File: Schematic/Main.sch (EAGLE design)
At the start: 68 parts, among them IC1 PIC18F4550_40, IC2 7805, IC4 AD7734, IC5 AD780, K1 SRD-24VDC-SL-C, K2 SRD-24VDC-SL-C, Q1 20MHz, Q2 3.579545MHz, T1 2N2222, U1 LM317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

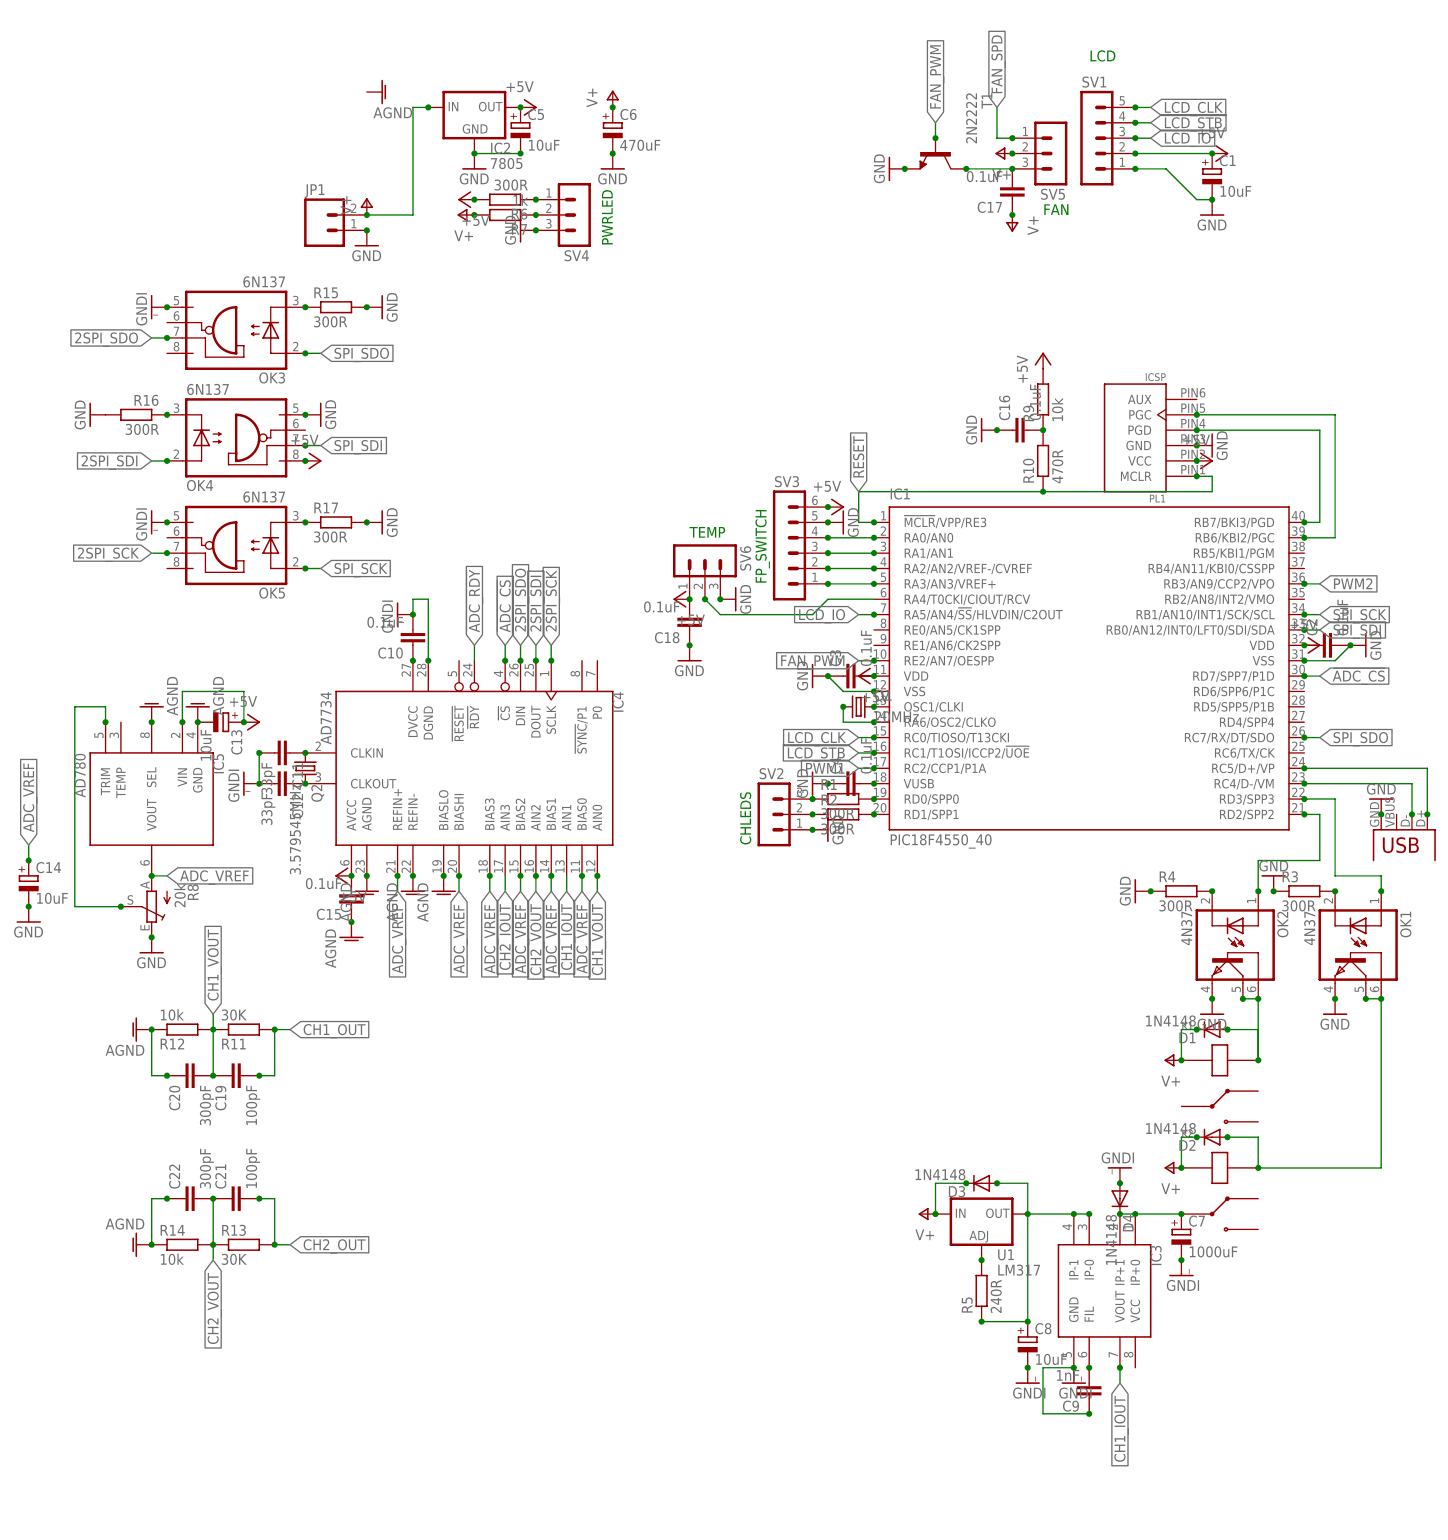
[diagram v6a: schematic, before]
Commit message: Added optocouplers to isolate output stuff; need separate PSU for µC stuff, second channel.
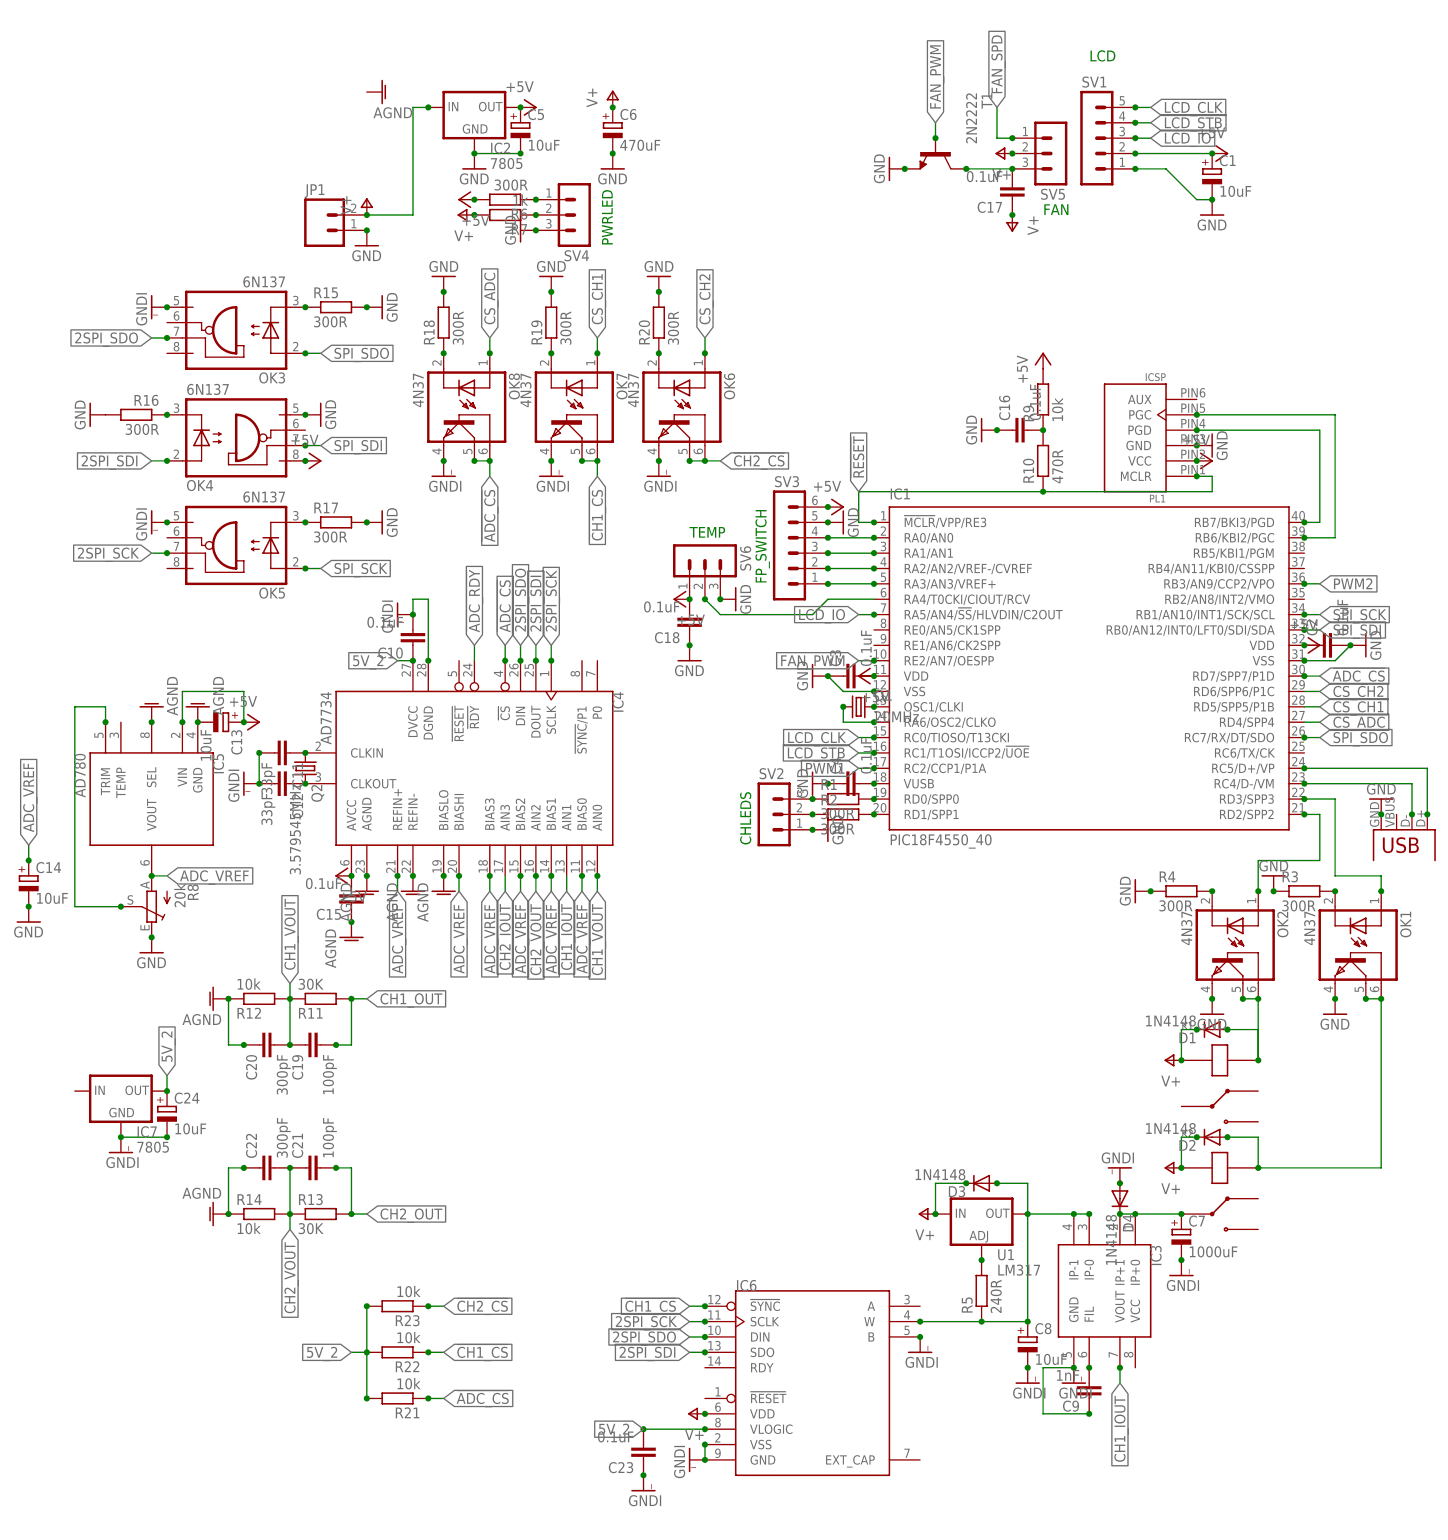
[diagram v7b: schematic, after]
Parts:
- added C23: 0.1uF, rcl:C-EU025-030X050
- added C24: 10uF, rcl:CPOL-EUE2.5-5
- added IC6: (no value), Particulates:AD5292TSSOP14
- added IC7: 7805, v-reg:78MXXS
- added OK6, OK7, OK8: 4N37, optocoupler:4N37
- added R18, R19, R20: 300R, rcl:R-EU_0204/7
- added R21, R22, R23: 10k, rcl:R-EU_0204/7
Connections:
- new net !CH1_CS!: IC6.!SYNC!, OK7.BAS, OK7.COL, R22.1
- new net !CH2_CS!: OK6.BAS, OK6.COL, R23.1
- new net 5V_2: C10.1, C23.2, C24.+, IC4.DVCC, IC6.VLOGIC, IC7.OUT, R21.2, R22.2, R23.2
- new net CS_ADC: IC1.RD4/SPP4, OK8.A
- new net CS_CH1: IC1.RD5/SPP5/P1B, OK7.A
- new net CS_CH2: IC1.RD6/SPP6/P1C, OK6.A
- new net N$36: OK8.C, R18.1
- new net N$37: OK7.C, R19.1
- new net N$38: OK6.C, R20.1
- net !ADC_CS!: now also OK8.BAS, OK8.COL, R21.1
- net +5V: no longer C10.1, IC4.DVCC
- net 2SPI_SCK: now also IC6.SCLK
- net 2SPI_SDI: now also IC6.SDO
- net 2SPI_SDO: now also IC6.DIN
- net GND: now also R18.2, R19.2, R20.2
- net GNDI: now also C23.1, C24.-, IC6.B, IC6.GND, IC6.VSS, IC7.GND, OK6.EMI, OK7.EMI, OK8.EMI
- net N$26: now also IC6.W
- net V+: now also IC6.VDD
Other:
- moved on the sheet: C19, C20, C21, C22, R11, R12, R13, R14

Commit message: Fixed LM317 bias resistor, added second 7805, etc.
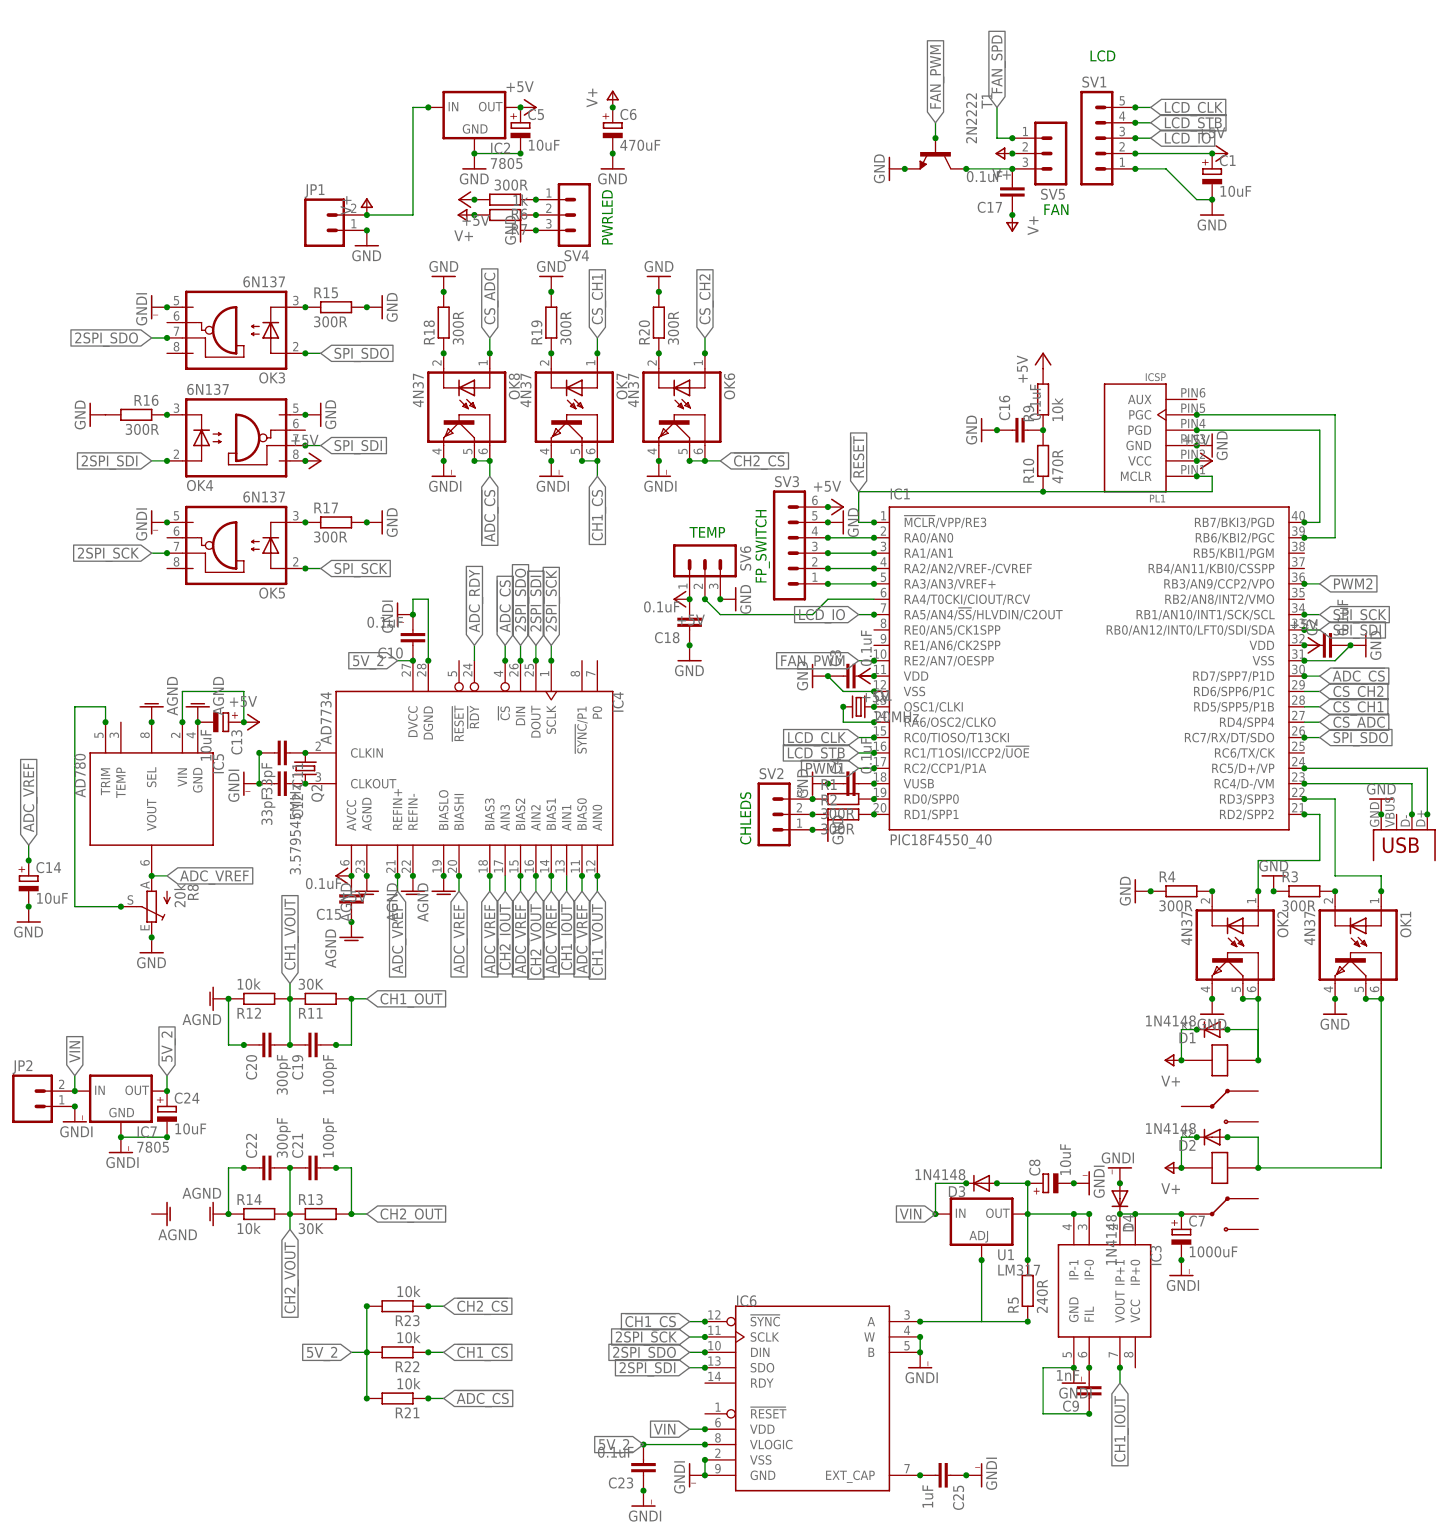
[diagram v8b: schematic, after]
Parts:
- added C25: 1uF, rcl:C-EU025-030X050
- added JP2: (no value), SparkFun:M023.5MM
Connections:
- removed net N$23: R5.2, U1.ADJ
- new net N$39: C25.2, IC6.EXT_CAP
- new net N$40: IC6.A, R5.1, U1.ADJ
- new net VIN: D3.C, IC6.VDD, IC7.IN, JP2.2, U1.IN
- net GNDI: now also C25.1, IC6.W, JP2.1
- net N$26: now also R5.2; no longer IC6.W, R5.1
- net V+: no longer D3.C, IC6.VDD, U1.IN
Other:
- moved on the sheet: C23, C8, IC6, R5
